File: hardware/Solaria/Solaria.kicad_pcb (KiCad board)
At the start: 2 copper layers, 28 parts, among them J1 BATERIAS, J2 PANELSOLAR, J3 CONTROLVCC, Q1 2N3904, Q2 IRF9540N, Q3 2N3904, Q4 IRF9540N, Q5 IRF9540N, Q6 2N3904, Q7 2N3904, Q8 IRF9540N, U1 TP4056, U2 TP4056, U3 LM2596, U4 MT3608

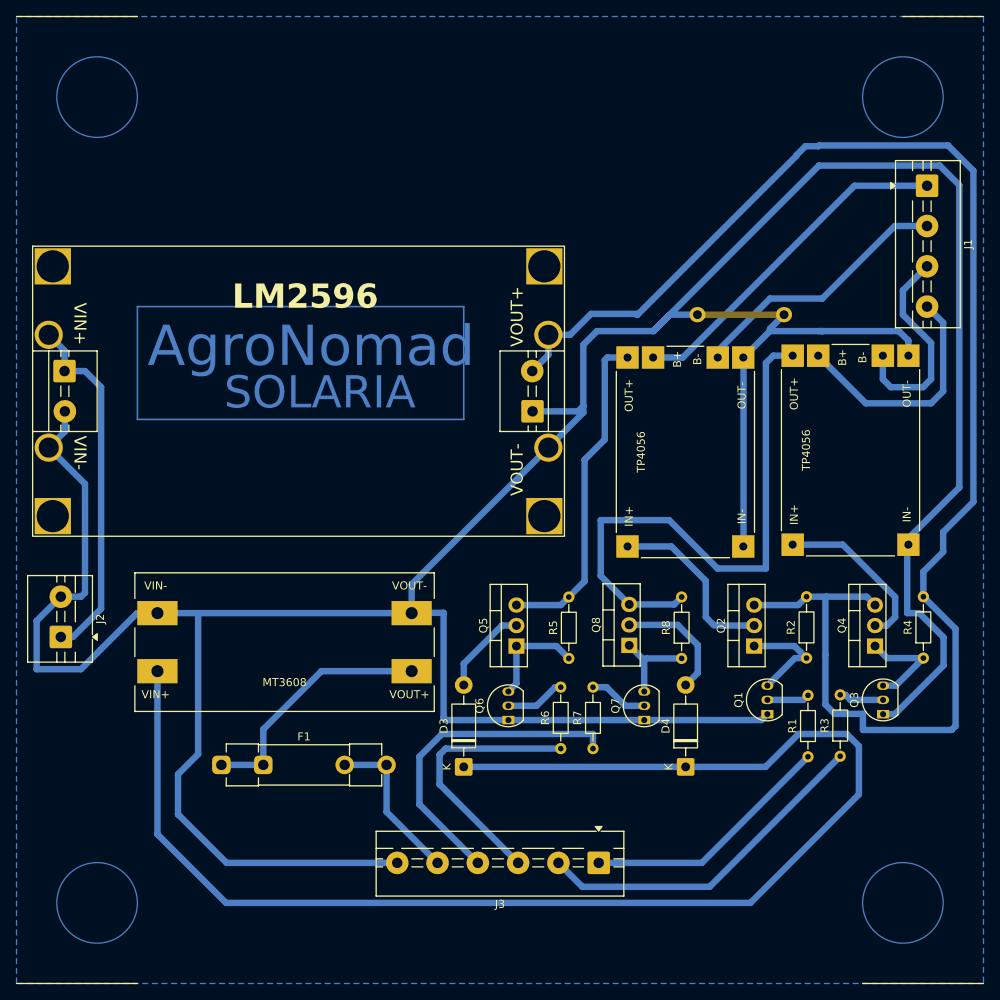
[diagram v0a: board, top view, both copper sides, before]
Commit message: feat: añadido de hardware, docs y firmware de ultima version
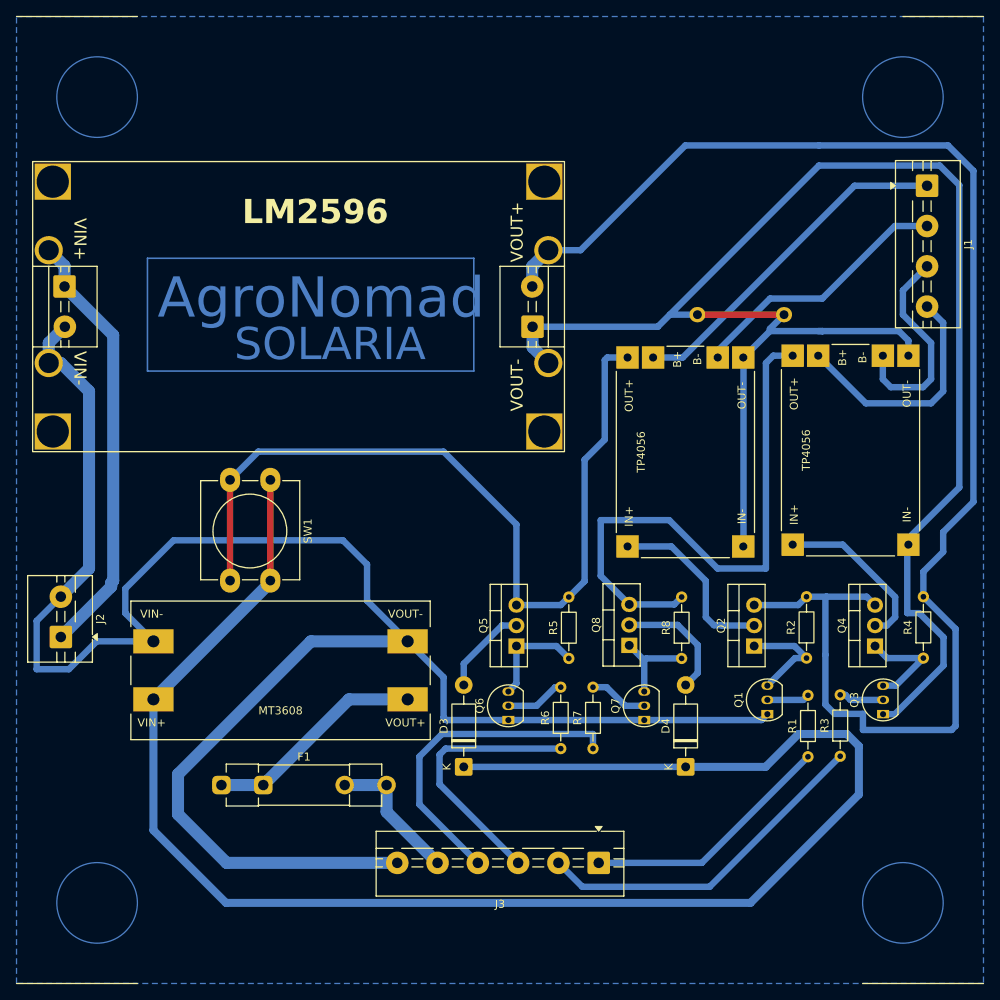
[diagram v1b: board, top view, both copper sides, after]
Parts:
- added SW1: SW_DPST_x2, Button_Switch_THT:SW_PUSH-12mm_Wuerth-430476085716, F.Cu at (61.5, 87.5)
- moved U3 10.5 mm to (65.0, 66.0)
- moved U4 3.54 mm to (62.8, 111.1)
- moved F1 2.50 mm to (55.4, 125.4)
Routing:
- net Net-(Q5-S): track 41.1 -> 104.4 mm
- net Net-(D3-K): track 173.8 -> 203.7 mm
- net Net-(J2-Pin_1): track 44.6 -> 54.0 mm
- net Net-(Q2-S): track 190.6 -> 186.0 mm
- net Net-(U4-VOUT+): track 31.0 -> 27.5 mm
- net SUOUT+: track 20.0 -> 17.5 mm
- net GND: track 450.5 -> 448.4 mm
